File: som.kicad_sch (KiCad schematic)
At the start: 63 parts, among them M1 SC606T

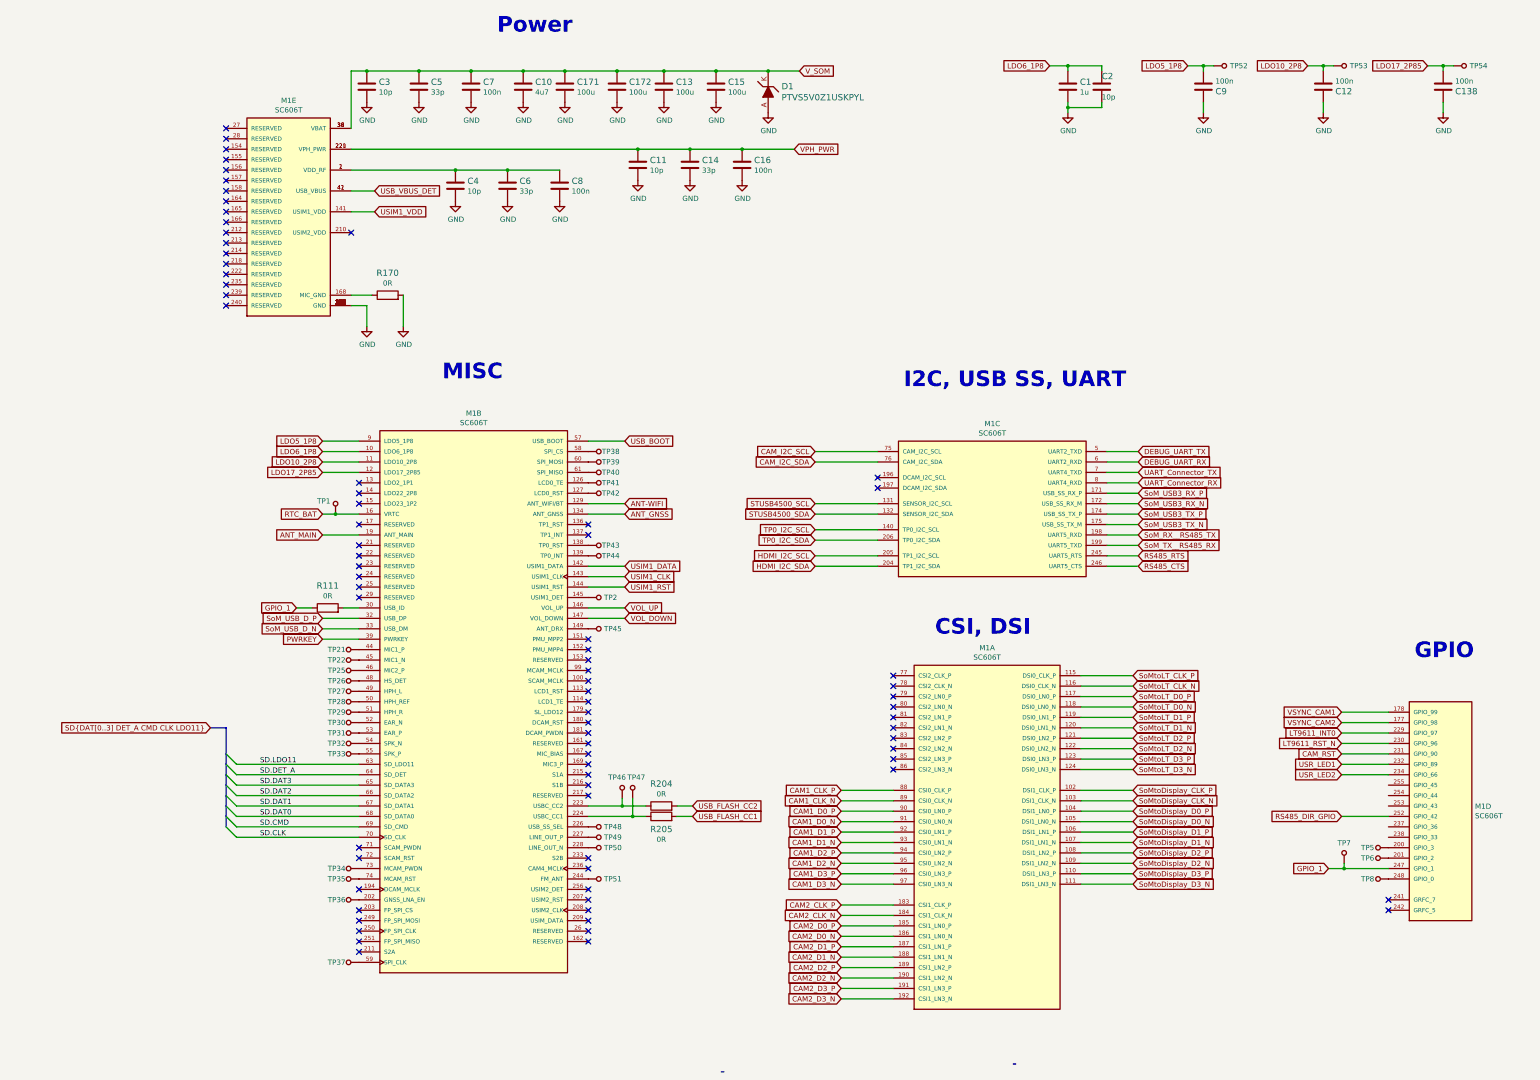
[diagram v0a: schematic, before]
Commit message: Introduce component standardization
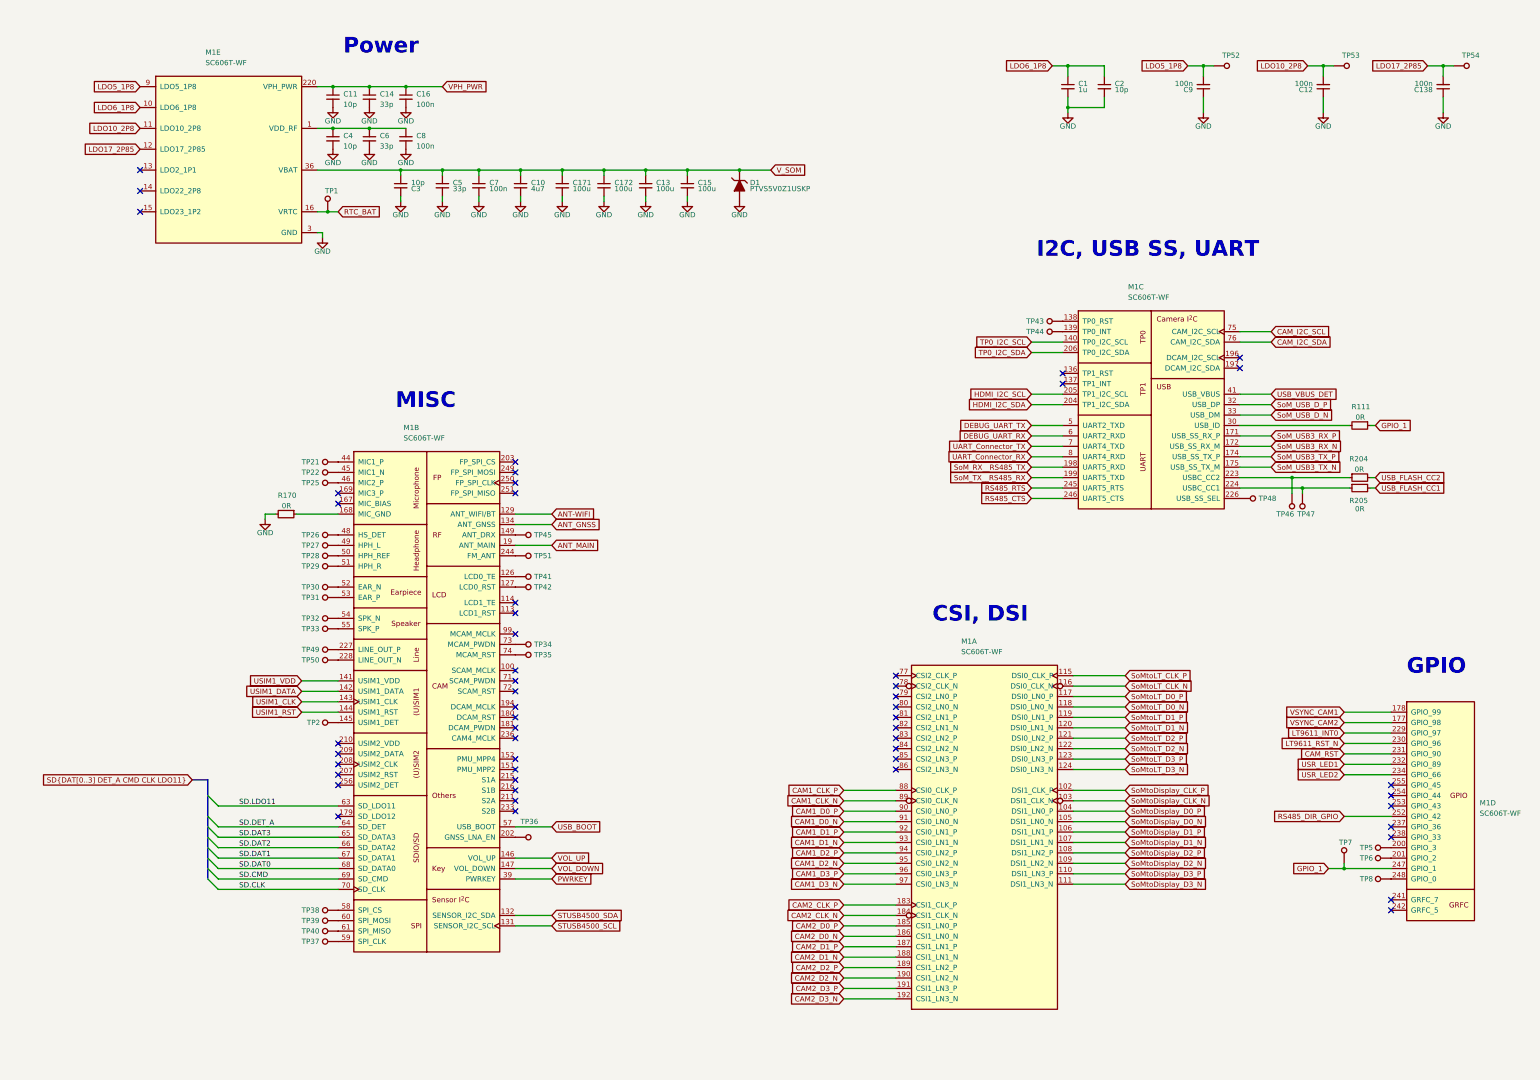
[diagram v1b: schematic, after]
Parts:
- C1: footprint sc606-baseboard-footprints:0402-cap -> sc606-baseboard-footprints:C_0402_1005Metric; Author (none) -> Antmicro; License (none) -> Apache-2.0
- C10: footprint sc606-baseboard-footprints:0402-cap -> sc606-baseboard-footprints:C_0402_1005Metric; Author (none) -> Antmicro; License (none) -> Apache-2.0; Manufacturer MURATA -> Murata
- C11, C2, C3, C4: footprint sc606-baseboard-footprints:0402-cap -> sc606-baseboard-footprints:C_0402_1005Metric; Author (none) -> Antmicro; Dielectric (none) -> C0G; License (none) -> Apache-2.0; MPN MC0402N100D500CT -> GCM1555C1H100GA16D; Manufacturer MULTICOMP -> Murata; Voltage (none) -> 50V
- C12, C138, C16, C7, C8, C9: footprint sc606-baseboard-footprints:0402-cap -> sc606-baseboard-footprints:C_0402_1005Metric; Author (none) -> Antmicro; Dielectric (none) -> X5R; License (none) -> Apache-2.0; MPN 0402X104K6R3CT -> GRM155R61H104KE14D; Manufacturer Walsin -> Murata; Voltage (none) -> 50V
- C13, C15, C171, C172: footprint sc606-baseboard-footprints:1206-cap -> sc606-baseboard-footprints:C_1206_3216Metric; Author (none) -> Antmicro; License (none) -> Apache-2.0
- C14, C5, C6: footprint sc606-baseboard-footprints:0402-cap -> sc606-baseboard-footprints:C_0402_1005Metric; Author (none) -> Antmicro; License (none) -> Apache-2.0; Manufacturer MULTICOMP -> Multicomp
- D1: value PTVS5V0Z1USKPYL -> PTVS5V0Z1USKP; symbol sc606-baseboard:PTVS5V0Z1USKPYL -> sc606-baseboard:PTVS5V0Z1USKP; Author (none) -> Antmicro; License (none) -> Apache-2.0
- M1: footprint sc606-baseboard-footprints:QUECTEL_SC606T -> sc606-baseboard-footprints:Quectel_SC606T; Author (none) -> Antmicro; License (none) -> Apache-2.0; MPN SC606T-xx -> SC606T-WF
- R111, R170, R204, R205: footprint sc606-baseboard-footprints:0402-res -> sc606-baseboard-footprints:R_0402_1005Metric; Author (none) -> Antmicro; Current (none) -> 1A; License (none) -> Apache-2.0; Manufacturer PANASONIC -> Panasonic
- TP1, TP2, TP21, TP22, TP25, TP26, TP27, TP28, TP29, TP30, TP31, TP32, TP33, TP34, TP35, TP36, TP37, TP38, TP39, TP40, TP41, TP42, TP43, TP44, TP45, TP46, TP47, TP48, TP49, TP5, TP50, TP51, TP52, TP53, TP54, TP6, TP7, TP8: value TP_SMD_1_5MM -> TP_1.5mm_SMD; footprint sc606-baseboard-footprints:TP-R-1.5 -> sc606-baseboard-footprints:TP_SMD_1.5mm; symbol sc606-baseboard:TP_SMD_0_75MM -> sc606-baseboard:TP_1.5mm_SMD; Author (none) -> Antmicro; License (none) -> Apache-2.0
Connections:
- net LDO10_2P8: now also M1.11 (LDO10_2P8); no longer M1.11 (LDO10_2P8)
- net LDO17_2P85: now also M1.12 (LDO17_2P85); no longer M1.12 (LDO17_2P85)
- net LDO5_1P8: now also M1.9 (LDO5_1P8); no longer M1.9 (LDO5_1P8)
- net LDO6_1P8: now also M1.10 (LDO6_1P8); no longer M1.10 (LDO6_1P8)
- net RTC_BAT: now also M1.16 (VRTC); no longer M1.16 (VRTC)
- net STUSB4500_SCL: now also M1.131 (SENSOR_I2C_SCL); no longer M1.131 (SENSOR_I2C_SCL)
- net STUSB4500_SDA: now also M1.132 (SENSOR_I2C_SDA); no longer M1.132 (SENSOR_I2C_SDA)
- net SoM_USB_D_N: now also M1.33 (USB_DM); no longer M1.33 (USB_DM)
- net SoM_USB_D_P: now also M1.32 (USB_DP); no longer M1.32 (USB_DP)
- net USB_VBUS_DET: now also M1.41 (USB_VBUS), M1.42 (USB_VBUS); no longer M1.41 (USB_VBUS), M1.42 (USB_VBUS)
- net USIM1_VDD: now also M1.141 (USIM1_VDD); no longer M1.141 (USIM1_VDD)
- net at TP43.1: now also M1.138 (TP0_RST); no longer M1.138 (TP0_RST)
- net at TP44.1: now also M1.139 (TP0_INT); no longer M1.139 (TP0_INT)
- net at R204.1, TP46.1: now also M1.223 (USBC_CC2); no longer M1.223 (USBC_CC2)
- net at R205.1, TP47.1: now also M1.224 (USBC_CC1); no longer M1.224 (USBC_CC1)
- net at TP48.1: now also M1.226 (USB_SS_SEL); no longer M1.226 (USB_SS_SEL)
- net at R111.2: now also M1.30 (USB_ID); no longer M1.30 (USB_ID)
- net at R170.1: now also M1.168 (MIC_GND); no longer M1.168 (MIC_GND)
- no-connect marks 77 -> 52
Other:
- moved on the sheet: C1, C10, C11, C12, C13, C138, C14, C15, C16, C171, C172, C2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

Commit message: [#61796] Run globlib
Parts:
- C1: footprint sc606-baseboard-footprints:C_0402_1005Metric -> antmicro-footprints:C_0402_1005Metric; symbol sc606-baseboard:C_1u_0402 -> antmicroCapacitors0402:C_1u_0402
- C10: footprint sc606-baseboard-footprints:C_0402_1005Metric -> antmicro-footprints:C_0402_1005Metric; symbol sc606-baseboard:C_4u7_0402 -> antmicroCapacitors0402:C_4u7_0402
- C11, C2, C3, C4: footprint sc606-baseboard-footprints:C_0402_1005Metric -> antmicro-footprints:C_0402_1005Metric; symbol sc606-baseboard:C_10p_0402 -> antmicroCapacitors0402:C_10p_0402
- C12, C138, C16, C7, C8, C9: footprint sc606-baseboard-footprints:C_0402_1005Metric -> antmicro-footprints:C_0402_1005Metric; symbol sc606-baseboard:C_100n_0402 -> antmicroCapacitors0402:C_100n_0402
- C13, C15, C171, C172: footprint sc606-baseboard-footprints:C_1206_3216Metric -> antmicro-footprints:C_1206_3216Metric; symbol sc606-baseboard:C_100u_1206 -> antmicroCapacitorsmisc:C_100u_1206
- C14, C5, C6: footprint sc606-baseboard-footprints:C_0402_1005Metric -> antmicro-footprints:C_0402_1005Metric; symbol sc606-baseboard:C_33p_0402 -> antmicroCapacitors0402:C_33p_0402
- D1: footprint sc606-baseboard-footprints:SOD-964 -> antmicro-footprints:D_SOD-964; symbol sc606-baseboard:PTVS5V0Z1USKP -> antmicroTVSDiodes:PTVS5V0Z1USKP
- M1: footprint sc606-baseboard-footprints:Quectel_SC606T -> antmicro-footprints:Quectel_SC606T; symbol sc606-baseboard:SC606T -> antmicroModules:SC606T
- R111, R170, R204, R205: footprint sc606-baseboard-footprints:R_0402_1005Metric -> antmicro-footprints:R_0402_1005Metric; symbol sc606-baseboard:R_0R_0402 -> antmicroResistors0402:R_0R_0402
- TP1, TP2, TP21, TP22, TP25, TP26, TP27, TP28, TP29, TP30, TP31, TP32, TP33, TP34, TP35, TP36, TP37, TP38, TP39, TP40, TP41, TP42, TP43, TP44, TP45, TP46, TP47, TP48, TP49, TP5, TP50, TP51, TP52, TP53, TP54, TP6, TP7, TP8: footprint sc606-baseboard-footprints:TP_SMD_1.5mm -> antmicro-footprints:TP_SMD_1.5mm; symbol sc606-baseboard:TP_1.5mm_SMD -> antmicroTestPoints:TP_1.5mm_SMD

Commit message: [#61796] Update schematics
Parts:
- C13, C15, C171, C172: MPN TMCMA0J107MTRF -> GRM31CR60J107MEA8K; Manufacturer Vishay -> Murata
- C14, C5, C6: MPN MC0402N330J500CT -> 04025A330FAT2A; Manufacturer Multicomp -> KYOCERA AVX
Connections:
- net GND: now also D1.2 (A); no longer D1.A
- net V_SOM: now also D1.1 (C); no longer D1.K
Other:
- company: (none) -> Antmicro Ltd

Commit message: [#61796] Update designators
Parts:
- renumbered M1 to U19
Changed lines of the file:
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@@
   (symbol (lib_id "antmicroModules:SC606T") (at 232.41 181.61 0) (unit 1)
     (in_bom yes) (on_board yes) (dnp no) (fields_autoplaced)
-    (property "Reference" "M1" (at 254 173.99 0)
+    (property "Reference" "U19" (at 254 173.99 0)
       (effects (font (size 1.27 1.27)))
     )
@@
       (project "sc606-baseboard"
         (path "/d033de6c-b5da-4924-ae5b-c5bab6f8ca2c/00000000-0000-0000-0000-000061d43102"
-          (reference "M1") (unit 1)
+          (reference "U19") (unit 1)
         )
       )
@@
   (symbol (lib_id "antmicroModules:SC606T") (at 96.52 129.54 0) (unit 2)
     (in_bom yes) (on_board yes) (dnp no) (fields_autoplaced)
-    (property "Reference" "M1" (at 118.11 121.92 0)
+    (property "Reference" "U19" (at 118.11 121.92 0)
       (effects (font (size 1.27 1.27)))
     )
@@
       (project "sc606-baseboard"
         (path "/d033de6c-b5da-4924-ae5b-c5bab6f8ca2c/00000000-0000-0000-0000-000061d43102"
-          (reference "M1") (unit 2)
+          (reference "U19") (unit 2)
         )
       )
@@
   (symbol (lib_id "antmicroModules:SC606T") (at 273.05 95.25 0) (unit 3)
     (in_bom yes) (on_board yes) (dnp no) (fields_autoplaced)
-    (property "Reference" "M1" (at 294.64 87.63 0)
+    (property "Reference" "U19" (at 294.64 87.63 0)
       (effects (font (size 1.27 1.27)))
     )
@@
       (project "sc606-baseboard"
         (path "/d033de6c-b5da-4924-ae5b-c5bab6f8ca2c/00000000-0000-0000-0000-000061d43102"
-          (reference "M1") (unit 3)
+          (reference "U19") (unit 3)
         )
       )
@@
   (symbol (lib_id "antmicroModules:SC606T") (at 353.06 190.5 0) (unit 4)
     (in_bom yes) (on_board yes) (dnp no) (fields_autoplaced)
-    (property "Reference" "M1" (at 374.65 213.36 0)
+    (property "Reference" "U19" (at 374.65 213.36 0)
       (effects (font (size 1.27 1.27)) (justify left))
     )
@@
       (project "sc606-baseboard"
         (path "/d033de6c-b5da-4924-ae5b-c5bab6f8ca2c/00000000-0000-0000-0000-000061d43102"
-          (reference "M1") (unit 4)
+          (reference "U19") (unit 4)
         )
       )
@@
   (symbol (lib_id "antmicroModules:SC606T") (at 48.26 38.1 0) (unit 5)
     (in_bom yes) (on_board yes) (dnp no) (fields_autoplaced)
-    (property "Reference" "M1" (at 69.85 30.48 0)
+    (property "Reference" "U19" (at 69.85 30.48 0)
       (effects (font (size 1.27 1.27)))
     )
@@
       (project "sc606-baseboard"
         (path "/d033de6c-b5da-4924-ae5b-c5bab6f8ca2c/00000000-0000-0000-0000-000061d43102"
-          (reference "M1") (unit 5)
+          (reference "U19") (unit 5)
         )
       )
